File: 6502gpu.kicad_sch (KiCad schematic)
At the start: 1 part, among them J1 DE15_Receptacle_HighDensity

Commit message: cleanup
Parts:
- added J2: Conn_01x14, symbol Connector_Generic:Conn_01x14
- added J3: Conn_01x08, symbol Connector_Generic:Conn_01x08
- added J4: Conn_01x01, symbol Connector_Generic:Conn_01x01
- added J5: Conn_01x02, symbol Connector_Generic:Conn_01x02
- added U32: 74HC00, symbol 74xx:74HC00
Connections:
- net A0: now also J2.1 (Pin_1)
- net A1: now also J2.2 (Pin_2)
- net A10: now also J2.11 (Pin_11)
- net A11: now also J2.12 (Pin_12)
- net A12: now also J2.13 (Pin_13)
- net A13: now also J2.14 (Pin_14)
- net A2: now also J2.3 (Pin_3)
- net A3: now also J2.4 (Pin_4)
- net A4: now also J2.5 (Pin_5)
- net A5: now also J2.6 (Pin_6)
- net A6: now also J2.7 (Pin_7)
- net A7: now also J2.8 (Pin_8)
- net A8: now also J2.9 (Pin_9)
- net A9: now also J2.10 (Pin_10)
- net Counters/VBlank: now also U32.1
- net GND: now also J5.2 (Pin_2)
- new net +5V: J5.1 (Pin_1)
- new net D0: J3.1 (Pin_1)
- new net D1: J3.2 (Pin_2)
- new net D2: J3.3 (Pin_3)
- new net D3: J3.4 (Pin_4)
- new net D4: J3.5 (Pin_5)
- new net D5: J3.6 (Pin_6)
- new net D6: J3.7 (Pin_7)
- new net D7: J3.8 (Pin_8)
- new net ~{NMI}: J4.1 (Pin_1), U32.3
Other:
- sheet Counters ports: added Col[0..9], Row[0..9]; removed Col, Row
- sheet DAC ports: added BlankBlack, BlankWhite, Blue, Green, HBlank, Pixel, Red, VBlank; removed none
- sheet Memory ports: added AddrCPU[0..14], AddrGPU[0..14], DataCPU[0..7], DataGPU[0..7]; removed AddrCPU, AddrGPU, DataCPU, DataGPU
- note added: "Address Bus"
- note added: "Data Bus"
- moved on the sheet: J1

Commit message: remove 3390, cleanup
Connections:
- net A0 renamed AddrCPU0
- net A1 renamed AddrCPU1
- net A10 renamed AddrCPU10
- net A11 renamed AddrCPU11
- net A12 renamed AddrCPU12
- net A13 renamed AddrCPU13
- net A2 renamed AddrCPU2
- net A3 renamed AddrCPU3
- net A4 renamed AddrCPU4
- net A5 renamed AddrCPU5
- net A6 renamed AddrCPU6
- net A7 renamed AddrCPU7
- net A8 renamed AddrCPU8
- net A9 renamed AddrCPU9
- net Blue renamed DAC/Blue
- net D0 renamed DataCPU0
- net D1 renamed DataCPU1
- net D2 renamed DataCPU2
- net D3 renamed DataCPU3
- net D4 renamed DataCPU4
- net D5 renamed DataCPU5
- net D6 renamed DataCPU6
- net D7 renamed DataCPU7
- net Green renamed DAC/Green
- net HSync renamed Counters/HSync
- net Red renamed DAC/Red
- net VSync renamed Counters/VSync
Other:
- sheet ConfigReg ports: added DataCPU[0..7]; removed DataIn
- sheet DAC ports: added PixelOut[0..7]; removed Pixel
- sheet Memory ports: added Col[0..9], PixelOut[0..7], Row[2..9]; removed AddrGPU[0..14], DataGPU[0..7]
- moved on the sheet: J1, J2, J3, J4, U32A

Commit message: work on DAC
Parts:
- removed J2: Conn_01x14, symbol Connector_Generic:Conn_01x14
- added J2: Conn_01x03, symbol Connector_Generic:Conn_01x03
- added J6: Conn_01x02, symbol Connector_Generic:Conn_01x02
- added J7: Conn_01x16, symbol Connector_Generic:Conn_01x16
- added U6: 74HC86, symbol 74xx:74HC86
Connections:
- net AddrCPU0: now also J7.1 (Pin_1)
- net AddrCPU1: now also J7.2 (Pin_2)
- net AddrCPU10: now also J7.11 (Pin_11)
- net AddrCPU11: now also J7.12 (Pin_12)
- net AddrCPU12: now also J7.13 (Pin_13)
- net AddrCPU13: now also J7.14 (Pin_14)
- net AddrCPU2: now also J7.3 (Pin_3)
- net AddrCPU3: now also J7.4 (Pin_4)
- net AddrCPU4: now also J7.5 (Pin_5)
- net AddrCPU5: now also J7.6 (Pin_6)
- net AddrCPU6: now also J7.7 (Pin_7)
- net AddrCPU7: now also J7.8 (Pin_8)
- net AddrCPU8: now also J7.9 (Pin_9)
- net AddrCPU9: now also J7.10 (Pin_10)
- net at U32.4: now also U6.3
- net at U32.5: now also J2.2 (Pin_2)
- net ~{EnableCPU}: now reaches U32.6
- new net AddrPhys14: J2.1 (Pin_1), J7.15 (Pin_15), U6.1
- new net AddrPhys15: J2.3 (Pin_3), J7.16 (Pin_16), U6.2
- new net ~{CpuClock}: J6.1 (Pin_1)
- new net ~{CpuWe}: J6.2 (Pin_2)
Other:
- moved on the sheet: J5, U32B, U32E

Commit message: work on main page layout
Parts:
- added U35: 74LV27, symbol 74xx:74LS27
- added U9: 74LS08, symbol 74xx:74LS08
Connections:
- net AddrCPU5: now also U32.12
- net AddrCPU7: now also U32.13
- net ConfigReg/BlankBlack: now also U35.13
- net ConfigReg/NmiEnable: now also U32.2
- net Counters/HBlank: now also U35.1
- net Counters/VBlank: now also U35.2
- net ~{CpuClock}: now also U35.4
- net ~{CpuWe}: now also U35.5
- net ~{EnableCPU}: now also U35.3
- net at U32.10: now also U32.9, U35.6
- net WriteMem: now reaches U32.8
- net ~{WriteReg}: now reaches U32.11
- net Counters/HSync renamed HSync
- net Counters/VSync renamed VSync
- net DataCPU0 renamed DataIn0
- net DataCPU1 renamed DataIn1
- net DataCPU2 renamed DataIn2
- net DataCPU3 renamed DataIn3
- net DataCPU4 renamed DataIn4
- net DataCPU5 renamed DataIn5
- net DataCPU6 renamed DataIn6
- net DataCPU7 renamed DataIn7
- new net DAC/~{BlankBlack}: U35.12
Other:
- sheet ConfigReg ports: added Clock, DataIn[0..7], ~{WriteReg}; removed DataCPU[0..7]
- sheet DAC ports: added ~{BlankBlack}; removed BlankBlack, HBlank, VBlank
- sheet Memory ports: added DataIn[0..7], Row[0..9], WriteMem; removed DataCPU[0..7], Row[2..9], WriteCPU
- note added: "160x120"
- note added: "Bit 0-7: Column Bit 8-13 + Bank: Row"
- note added: "Blue"
- note added: "Green"
- note added: "Red"
- moved on the sheet: J1, J2, J3, J4, U32A, U32B, U32C, U32D, U6A

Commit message: finish control logic?
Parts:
- removed U9: 74LS08, symbol 74xx:74LS08
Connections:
- net +5V: now also U32.14 (VCC), U35.14 (VCC), U6.14 (VCC), U6.4, U6.9
- net ConfigReg/Clock: now also U6.6
- net GND: now also U32.10, U32.7 (GND), U32.9, U35.7 (GND), U6.12, U6.13, U6.7 (GND)
- net WriteMem: now also U6.8; no longer U32.8
- net ~{CpuClock}: now also U6.5
- net ~{CpuWe}: now also U35.11
- net ~{EnableCPU}: now also U35.9
- net ~{WriteReg}: now also U35.8; no longer U32.11
- net ~{RegSel}: now reaches U35.10
- net ~{RegSel}: now also U32.11
- net at U6.10: now also U35.6
- no-connect marks 5 -> 7
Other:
- moved on the sheet: U32C, U32E, U35C, U35D, U6B, U6C, U6D, U6E

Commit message: misc fixes, start on pcb
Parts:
- removed unit 5 of U32
- removed unit 4 of U35
- removed unit 5 of U6
- added C35: 10u, Capacitor_SMD:C_1206_3216Metric_Pad1.33x1.80mm_HandSolder, symbol Device:C
- added J8, J9: Conn_01x02, Connector_PinHeader_2.54mm:PinHeader_1x02_P2.54mm_Vertical, symbol Connector_Generic:Conn_01x02
- J1: renamed from J6; footprint (none) -> Connector_PinHeader_2.54mm:PinHeader_1x02_P2.54mm_Vertical
- J2: renamed from J3; footprint (none) -> Connector_PinHeader_2.54mm:PinHeader_1x08_P2.54mm_Vertical
- J3: renamed from J5; footprint (none) -> Connector_PinHeader_2.54mm:PinHeader_1x02_P2.54mm_Vertical
- J4: renamed from J7; footprint (none) -> Connector_PinHeader_2.54mm:PinHeader_1x16_P2.54mm_Vertical
- J5: renamed from J4; footprint (none) -> Connector_PinHeader_2.54mm:PinHeader_1x01_P2.54mm_Vertical
- J6: renamed from J2; footprint (none) -> Connector_PinHeader_2.54mm:PinHeader_1x03_P2.54mm_Vertical
- J7: renamed from J1; footprint (none) -> footprints:CONN_L77HDE15SD1CH4FVGA_AMP
- U1: renamed from U6; footprint (none) -> Package_SO:SOIC-14_3.9x8.7mm_P1.27mm
- U2: renamed from U32; footprint (none) -> Package_SO:SOIC-14_3.9x8.7mm_P1.27mm
- U3: renamed from U35; footprint (none) -> Package_SO:SOIC-14_3.9x8.7mm_P1.27mm
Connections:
- net +5V: now also C35.1
- net GND: now also C35.2
- net WriteMem: now also U3.6; no longer U1.8
- net ~{WriteReg}: now also U1.8; no longer U3.8
- net AddrSelect: now reaches J6.2 (Pin_2), U2.5
- net at U1.10: now also U3.8; no longer U3.6
- net ConfigReg/Clock renamed ~{Phi2}
- net ~{Phi2}: now also U3.4
- net HSync: no longer names the net of J7.13
- net HSync: now also J9.2 (Pin_2)
- net VSync: no longer names the net of J7.14
- net VSync: now also J8.2 (Pin_2)
- net ~{CpuClock} renamed Phi2
- net Phi2: no longer U3.4
- net ~{CpuWe} renamed R~{W}
- new net ~{HSync}: J9.1 (Pin_1)
- new net ~{VSync}: J8.1 (Pin_1)
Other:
- added sheet Power (power.kicad_sch)
- sheet Counters ports: added ~{HSync}, ~{VSync}; removed HSync, VSync
- note added: "0x4000-0x7FFF"
- note added: "0x8000-0xBFFF"
- note added: "Jumper"
- moved on the sheet: J1, J3, J5, U1B, U1C, U2A, U2C

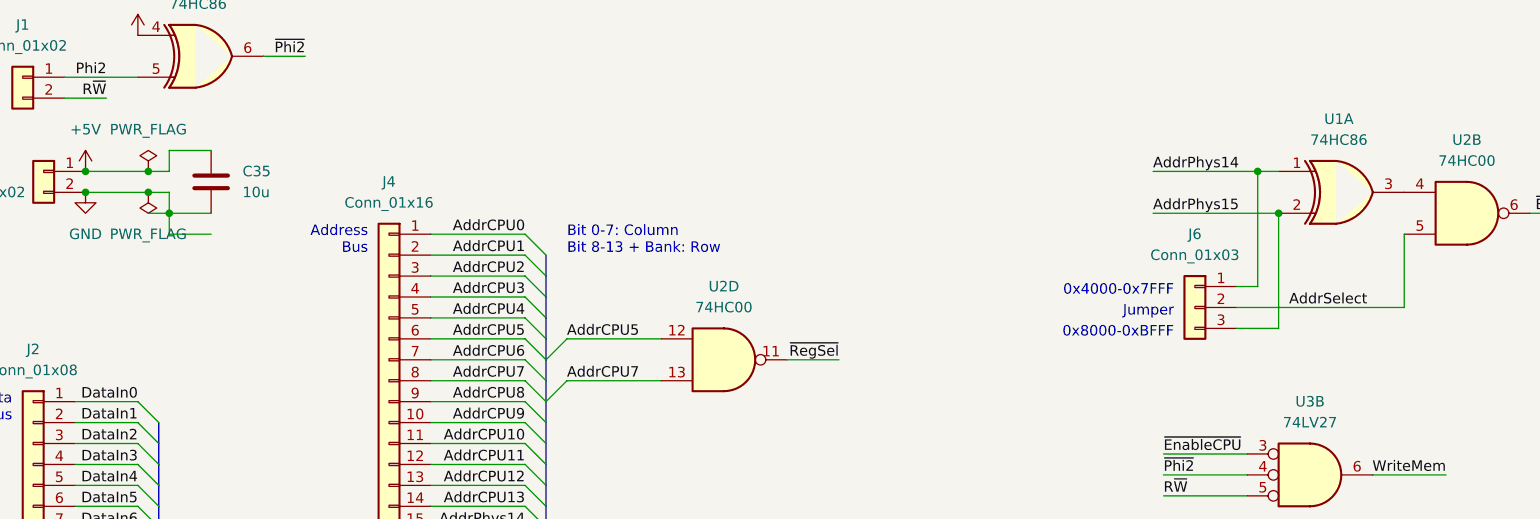
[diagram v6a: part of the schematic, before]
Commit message: fix and update verilog model
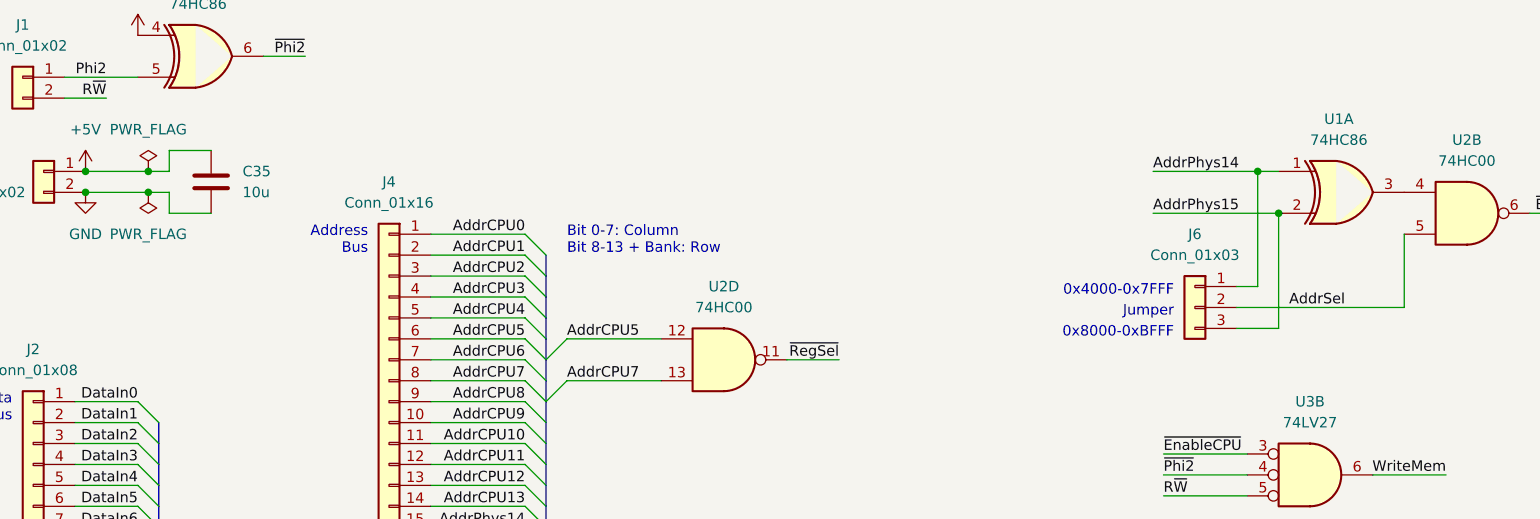
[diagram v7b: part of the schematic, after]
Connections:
- net AddrSelect renamed AddrSel
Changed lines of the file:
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@@
   (junction (at 34.29 43.18) (diameter 0) (color 0 0 0 0)
-  )
-  (junction (at 44.45 48.26) (diameter 0) (color 0 0 0 0)
   )
   (junction (at 179.07 48.26) (diameter 0) (color 0 0 0 0)
@@
     (stroke (width 0) (type default))
   )
-  (wire (pts (xy 44.45 50.8) (xy 49.53 50.8))
-    (stroke (width 0) (type default))
-  )
   (bus (pts (xy 43.18 91.44) (xy 43.18 96.52))
     (stroke (width 0) (type default))
@@
     (stroke (width 0) (type default))
   )
-  (wire (pts (xy 41.91 48.26) (xy 44.45 48.26))
-    (stroke (width 0) (type default))
-  )
   (bus (pts (xy 90.17 81.28) (xy 90.17 83.82))
     (stroke (width 0) (type default))
@@
     (stroke (width 0) (type default))
   )
-  (wire (pts (xy 44.45 48.26) (xy 44.45 50.8))
-    (stroke (width 0) (type default))
-  )
   (bus (pts (xy 43.18 101.6) (xy 45.72 101.6))
     (stroke (width 0) (type default))
@@
     (effects (font (size 1.27 1.27)) (justify right bottom))
   )
-  (label "AddrSelect" (at 180.34 59.69 0) (fields_autoplaced)
-    (effects (font (size 1.27 1.27)) (justify left bottom))
-  )
+  (label "AddrSel" (at 180.34 59.69 0) (fields_autoplaced)
+    (effects (font (size 1.27 1.27)) (justify left bottom))
+  )
